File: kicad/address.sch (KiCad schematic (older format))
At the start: 12 parts, among them SW6 Address, SW7 Program, U49 74LS173, U50 74LS157

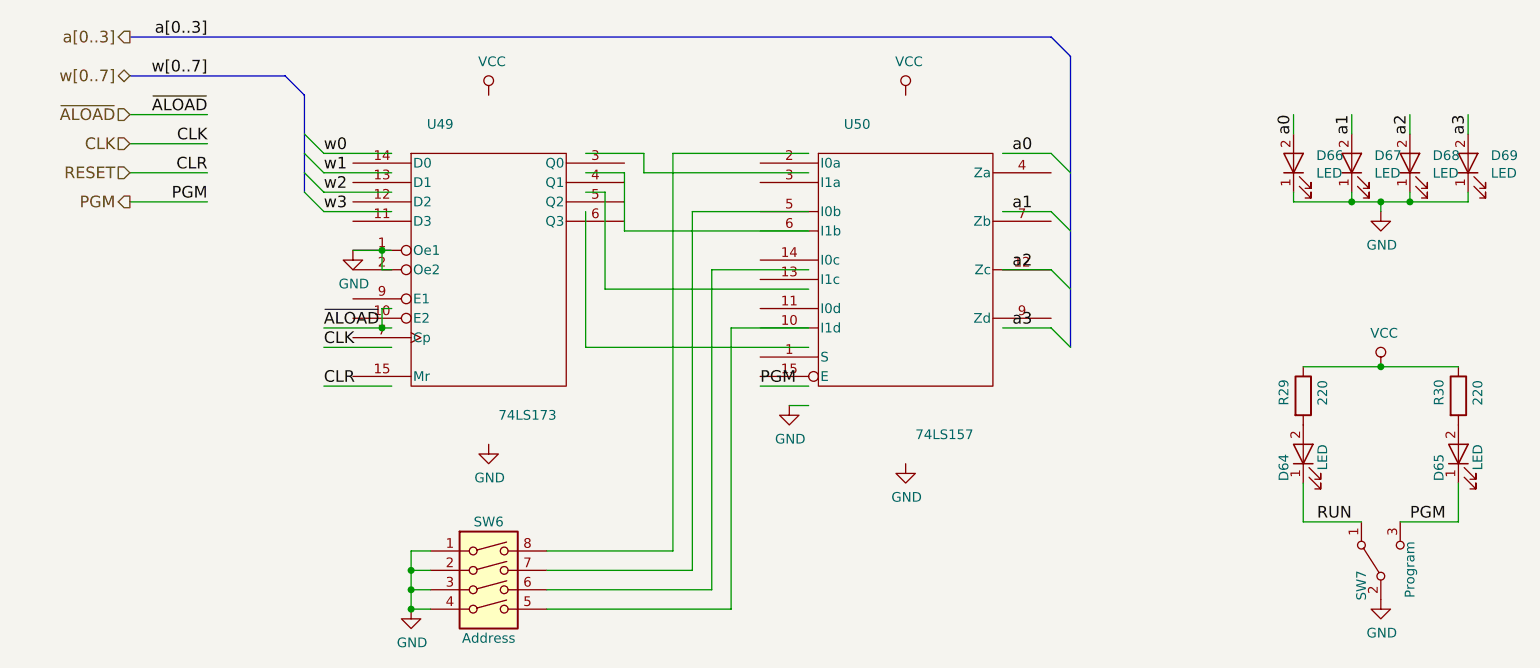
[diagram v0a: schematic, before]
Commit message: update bus names and improve sheet text
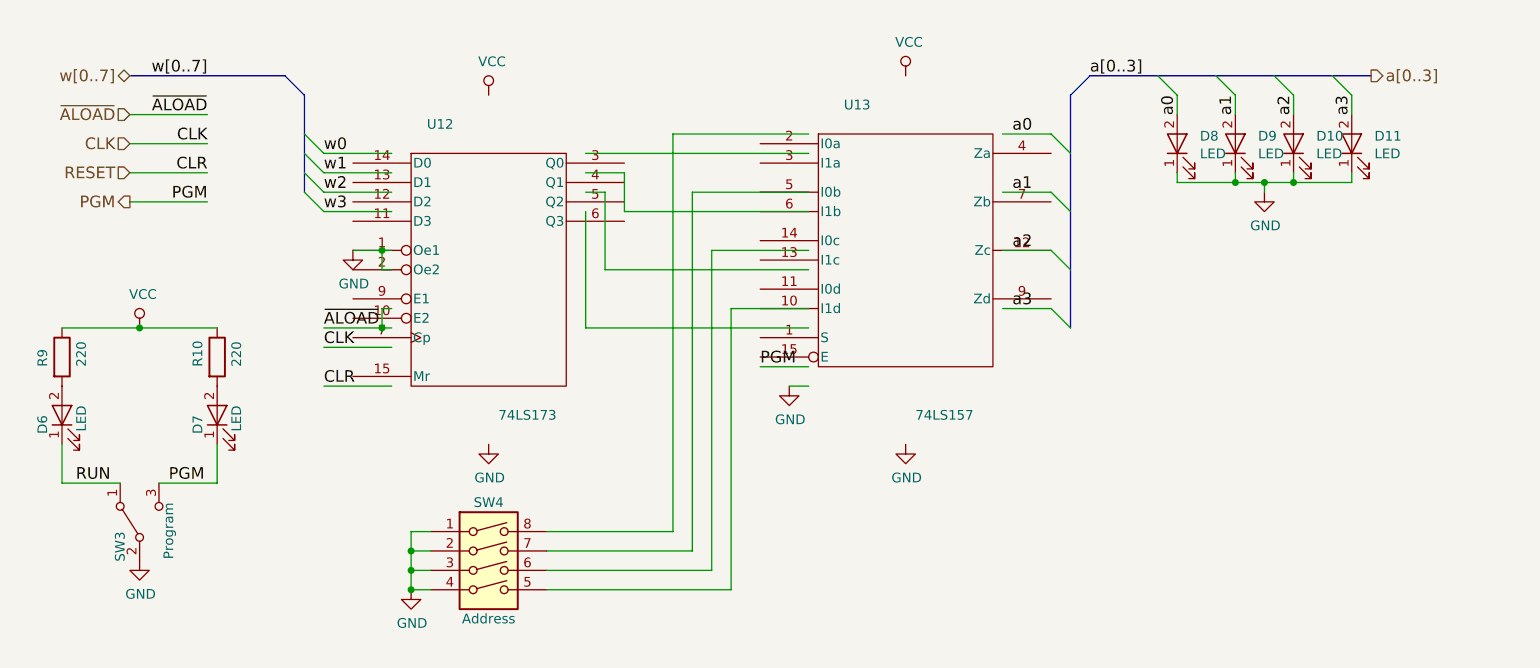
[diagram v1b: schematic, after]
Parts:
- renumbered D68 to D10, D69 to D11, D64 to D6, D65 to D7, D66 to D8, D67 to D9, R30 to R10, R29 to R9, SW7 to SW3, SW6 to SW4, U49 to U12, U50 to U13
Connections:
- wire segments 73 -> 71
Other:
- moved on the sheet: D10, D11, D6, D7, D8, D9, R10, R9, SW3, SW4, U13
